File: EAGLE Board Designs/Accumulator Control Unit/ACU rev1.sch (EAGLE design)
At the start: 177 parts, among them J1 CONNECTOR-CAN_MF_T_V_, J2 CONNECTOR-8_MF_T_V_, J3 CONNECTOR-8_MF_T_V_, J4 CONNECTOR-2_MF_T_V_, J5 CONNECTOR-12_MF_T_V_, Q1 TRANSISTOR_N_MOS__PMV15ENEA, Q2 TRANSISTOR_N_MOS__PMV15ENEA, T1 TRANSFORMER_HM2112ZNLT_AIRGAP, U10 OPAMP_1_CHANNEL_OPA991, U11 LOGICGATE_AND_DCK3, U12 OPAMP_1_CHANNEL_OPA991, U13 OPAMP_1_CHANNEL_OPA991, U14 OPAMP_1_CHANNEL_OPA991, U15 LOGICGATE_AND_DCK3, U18 OPAMP_1_CHANNEL_OPA991, U19 MAX7404, U2 ADG1423, U20 OPAMP_1_CHANNEL_OPA991, U22 OPAMP_1_CHANNEL_OPA991, U25 TCAN1051HQV-Q1, U26 MAX7404, U27 OPAMP_1_CHANNEL_OPA991, U28 MAX7404, U29 OPAMP_1_CHANNEL_OPA991, U3 LM555, U30 MAX7404, U4 OPAMP_1_CHANNEL_OPA991, U5 LTC6820, U6 ADM823, U7 OPAMP_1_CHANNEL_OPA991, U8 LOGICGATE_AND_DCK3, U9 OPAMP_1_CHANNEL_OPA991

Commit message: pack+ and ts+ filtering
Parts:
- added D14: LED_0603_GREEN, HyTechDevices - Copy:LED_0603_GREEN
- added R71: RESISTOR_0603_470, HyTechDevices - Copy:RESISTOR_0603_470
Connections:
- new net N$14: D14.A, R71.1
- net +3V3: now also R71.2
- net GND: now also D14.C
- net IMD_OK_TEENSY: now also A1.A2; no longer A1.A4
- net PACK+_FILTERED: now also A1.A4; no longer A1.A3
- net TEENSY_OK: now also A1.D4; no longer A1.D8
- net TS+_OUT_FILTERED: now also A1.A3; no longer A1.A2
- net WATCHDOG_INPUT: now also A1.D5; no longer A1.D9
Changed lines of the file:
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@@
 <part name="P9" library="HyTechSupplies" deviceset="GND" device=""/>
 <part name="P3" library="HyTechSupplies" deviceset="+12V" device=""/>
+<part name="P45" library="HyTechSupplies" deviceset="GND" device=""/>
+<part name="P44" library="HyTechSupplies" deviceset="+3V3" device=""/>
+<part name="D14" library="HyTechDevices - Copy" deviceset="LED_?_*" device="0603" technology="GREEN"/>
+<part name="R71" library="HyTechDevices - Copy" deviceset="RESISTOR_?_*" device="0603" technology="470"/>
 </parts>
 <sheets>
@@
 <attribute name="VALUE" x="53.34" y="120.65" size="1.27" layer="96" align="bottom-center"/>
 </instance>
+<instance part="P45" gate="1" x="238.76" y="170.18" smashed="yes">
+<attribute name="VALUE" x="238.76" y="168.91" size="1.27" layer="96" align="top-center"/>
+</instance>
+<instance part="P44" gate="G$1" x="238.76" y="203.2" smashed="yes">
+<attribute name="VALUE" x="238.76" y="204.47" size="1.27" layer="96" align="bottom-center"/>
+</instance>
+<instance part="D14" gate="LED" x="238.76" y="177.8" smashed="yes" rot="R270">
+<attribute name="COLOR" x="236.982" y="179.07" size="1.27" layer="95" rot="R270" align="top-center"/>
+<attribute name="NAME" x="242.316" y="179.07" size="1.27" layer="96" rot="R270" align="bottom-center"/>
+</instance>
+<instance part="R71" gate="G$1" x="238.76" y="193.04" smashed="yes" rot="R90">
+<attribute name="NAME" x="237.49" y="191.77" size="1.27" layer="95" rot="R90" align="bottom-center"/>
+<attribute name="RESISTANCE" x="240.03" y="191.77" size="1.27" layer="96" rot="R90" align="top-center"/>
+</instance>
 </instances>
 <busses>
@@
 <pinref part="U$1" gate="G$1" pin="6"/>
 </segment>
+<segment>
+<wire x1="238.76" y1="175.26" x2="238.76" y2="172.72" width="0.1524" layer="91"/>
+<pinref part="P45" gate="1" pin="GND"/>
+<pinref part="D14" gate="LED" pin="C"/>
+</segment>
 </net>
 <net name="+12V" class="0">
@@
 <pinref part="A3" gate="G$1" pin="OUT"/>
 </segment>
+<segment>
+<wire x1="238.76" y1="200.66" x2="238.76" y2="195.58" width="0.1524" layer="91"/>
+<pinref part="P44" gate="G$1" pin="+3V3"/>
+<pinref part="R71" gate="G$1" pin="2"/>
+</segment>
 </net>
 <net name="PRECHARGE_OK" class="0">
@@
 </segment>
 </net>
+<net name="N$14" class="0">
+<segment>
+<wire x1="238.76" y1="187.96" x2="238.76" y2="182.88" width="0.1524" layer="91"/>
+<pinref part="D14" gate="LED" pin="A"/>
+<pinref part="R71" gate="G$1" pin="1"/>
+</segment>
+</net>
 </nets>
 </sheet>
@@
 </segment>
 <segment>
-<pinref part="A1" gate="G$1" pin="A4"/>
-<wire x1="48.26" y1="160.02" x2="45.72" y2="160.02" width="0.1524" layer="91"/>
-<label x="45.72" y="160.02" size="1.27" layer="95" rot="R180" xref="yes"/>
+<wire x1="48.26" y1="165.1" x2="45.72" y2="165.1" width="0.1524" layer="91"/>
+<label x="45.72" y="165.1" size="1.27" layer="95" rot="R180" xref="yes"/>
+<pinref part="A1" gate="G$1" pin="A2"/>
 </segment>
 </net>
@@
 </segment>
 <segment>
-<pinref part="A1" gate="G$1" pin="D9"/>
-<wire x1="73.66" y1="162.56" x2="88.9" y2="162.56" width="0.1524" layer="91"/>
-<label x="88.9" y="162.56" size="1.27" layer="95" xref="yes"/>
+<wire x1="73.66" y1="152.4" x2="88.9" y2="152.4" width="0.1524" layer="91"/>
+<label x="88.9" y="152.4" size="1.27" layer="95" xref="yes"/>
+<pinref part="A1" gate="G$1" pin="D5"/>
 </segment>
 </net>
@@
 </segment>
 </net>
-<net name="TS+_OUT_FILTERED" class="0">
-<segment>
-<pinref part="A1" gate="G$1" pin="A2"/>
-<wire x1="48.26" y1="165.1" x2="43.18" y2="165.1" width="0.1524" layer="91"/>
-<label x="43.18" y="165.1" size="1.27" layer="95" rot="R180" xref="yes"/>
-</segment>
-</net>
-<net name="PACK+_FILTERED" class="0">
-<segment>
-<pinref part="A1" gate="G$1" pin="A3"/>
-<wire x1="48.26" y1="162.56" x2="45.72" y2="162.56" width="0.1524" layer="91"/>
-<label x="45.72" y="162.56" size="1.27" layer="95" rot="R180" xref="yes"/>
-</segment>
-</net>
 <net name="N$40" class="0">
 <segment>
@@
 <net name="TEENSY_OK" class="0">
 <segment>
-<pinref part="A1" gate="G$1" pin="D8"/>
-<wire x1="73.66" y1="160.02" x2="88.9" y2="160.02" width="0.1524" layer="91"/>
-<label x="88.9" y="160.02" size="1.27" layer="95" xref="yes"/>
-</segment>
-<segment>
 <pinref part="U6" gate="G$1" pin="!MR!"/>
 <wire x1="215.9" y1="91.44" x2="208.28" y2="91.44" width="0.1524" layer="91"/>
@@
 <label x="190.5" y="91.44" size="1.27" layer="95" rot="R180" xref="yes"/>
 </segment>
+<segment>
+<wire x1="73.66" y1="149.86" x2="88.9" y2="149.86" width="0.1524" layer="91"/>
+<label x="88.9" y="149.86" size="1.27" layer="95" xref="yes"/>
+<pinref part="A1" gate="G$1" pin="D4"/>
+</segment>
 </net>
 <net name="N$13" class="0">
@@
 </segment>
 </net>
+<net name="TS+_OUT_FILTERED" class="0">
+<segment>
+<wire x1="48.26" y1="162.56" x2="45.72" y2="162.56" width="0.1524" layer="91"/>
+<label x="45.72" y="162.56" size="1.27" layer="95" rot="R180" xref="yes"/>
+<pinref part="A1" gate="G$1" pin="A3"/>
+</segment>
+</net>
+<net name="PACK+_FILTERED" class="0">
+<segment>
+<wire x1="48.26" y1="160.02" x2="45.72" y2="160.02" width="0.1524" layer="91"/>
+<label x="45.72" y="160.02" size="1.27" layer="95" rot="R180" xref="yes"/>
+<pinref part="A1" gate="G$1" pin="A4"/>
+</segment>
+</net>

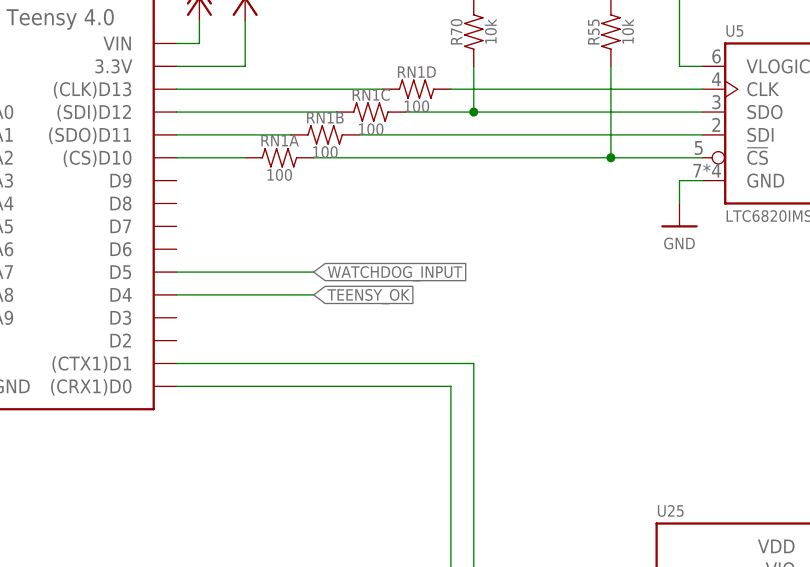
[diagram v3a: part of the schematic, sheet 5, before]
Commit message: routed shutdown optocouplers
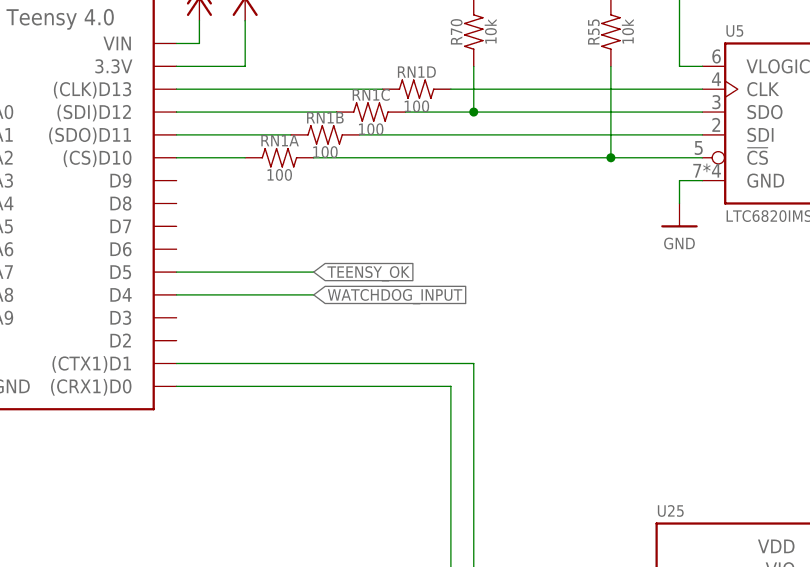
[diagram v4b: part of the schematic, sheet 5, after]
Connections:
- net TEENSY_OK: now also A1.D5; no longer A1.D4
- net WATCHDOG_INPUT: now also A1.D4; no longer A1.D5
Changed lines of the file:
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@@
 <drawing>
 <settings>
-<setting alwaysvectorfont="yes"/>
+<setting alwaysvectorfont="no"/>
 <setting verticaltext="up"/>
 </settings>
@@
 </segment>
 <segment>
-<wire x1="73.66" y1="152.4" x2="88.9" y2="152.4" width="0.1524" layer="91"/>
-<label x="88.9" y="152.4" size="1.27" layer="95" xref="yes"/>
-<pinref part="A1" gate="G$1" pin="D5"/>
+<wire x1="73.66" y1="149.86" x2="88.9" y2="149.86" width="0.1524" layer="91"/>
+<label x="88.9" y="149.86" size="1.27" layer="95" xref="yes"/>
+<pinref part="A1" gate="G$1" pin="D4"/>
 </segment>
 </net>
@@
 </segment>
 <segment>
-<wire x1="73.66" y1="149.86" x2="88.9" y2="149.86" width="0.1524" layer="91"/>
-<label x="88.9" y="149.86" size="1.27" layer="95" xref="yes"/>
-<pinref part="A1" gate="G$1" pin="D4"/>
+<wire x1="73.66" y1="152.4" x2="88.9" y2="152.4" width="0.1524" layer="91"/>
+<label x="88.9" y="152.4" size="1.27" layer="95" xref="yes"/>
+<pinref part="A1" gate="G$1" pin="D5"/>
 </segment>
 </net>

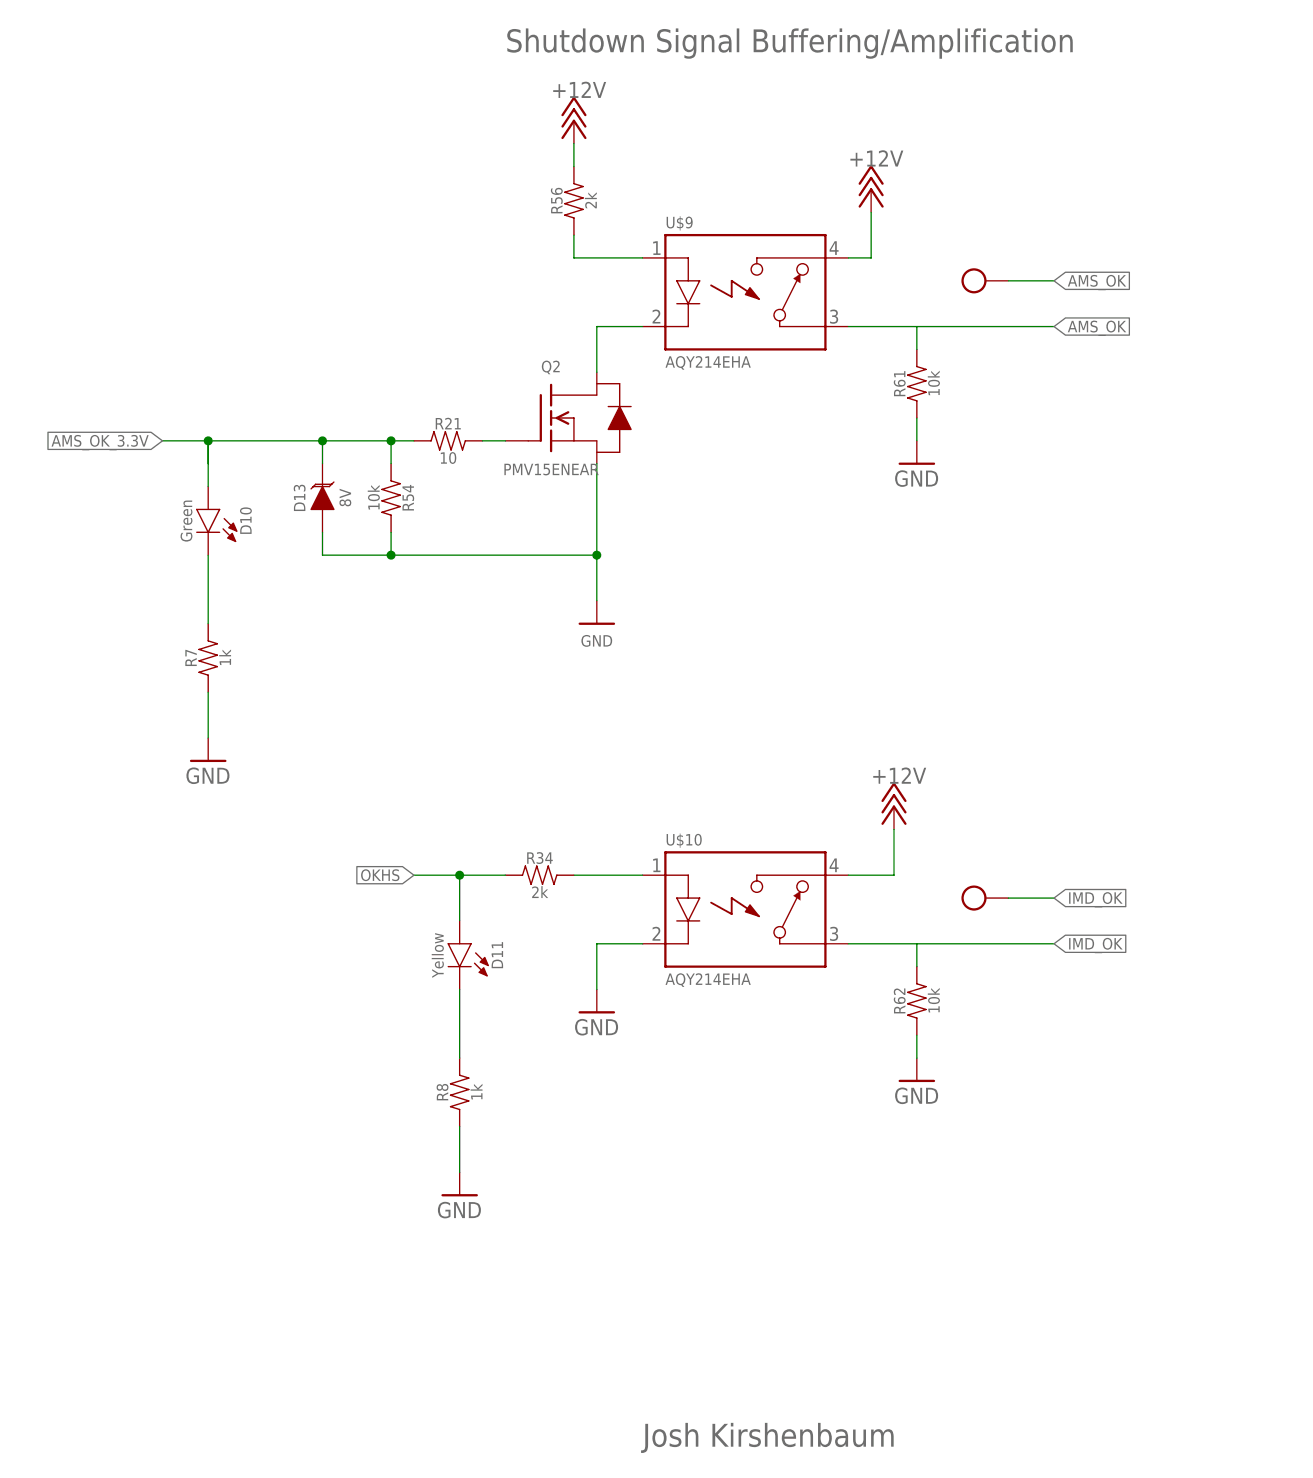
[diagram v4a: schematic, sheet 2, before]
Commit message: passes drc
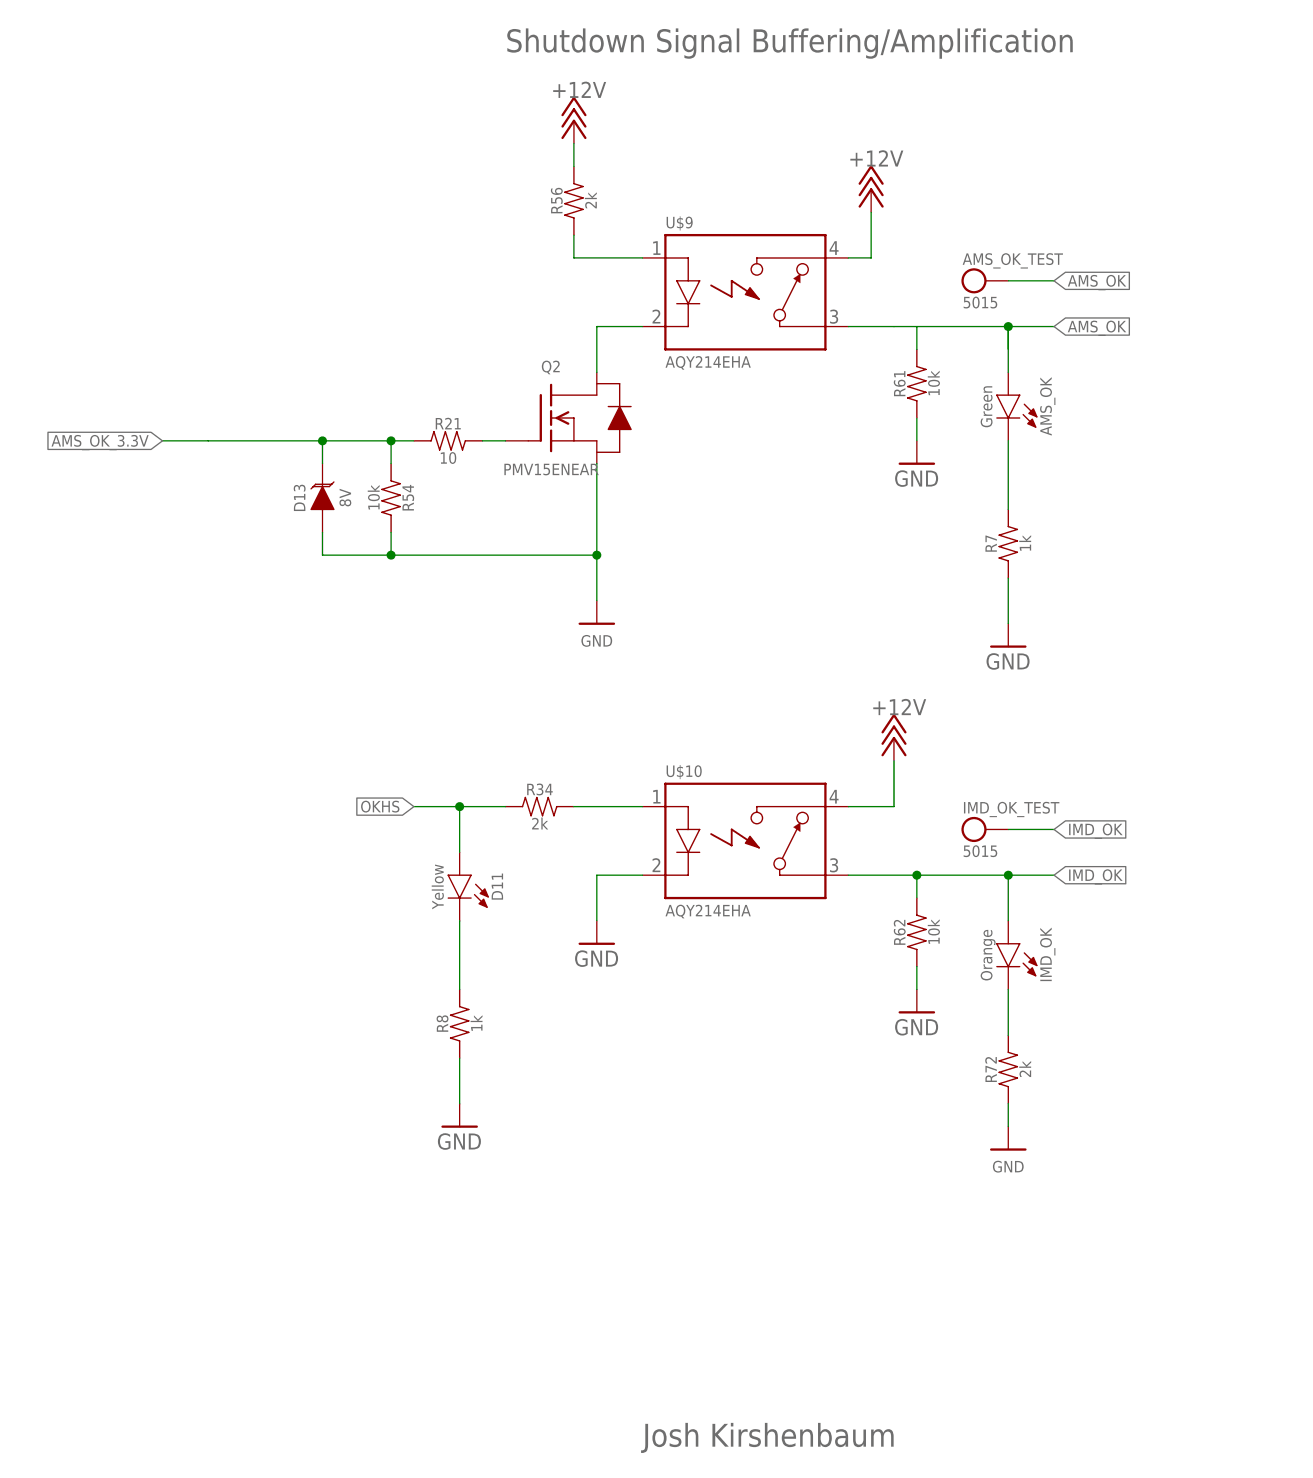
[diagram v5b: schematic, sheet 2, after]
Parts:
- removed $$U$12, U$13: TEST_POINTMICRO_MINIATURE, HyTechDevices:TEST_POINTMICRO_MINIATURE
- removed D10: LED_0603_GREEN, HyTechDevices - Copy:LED_0603_GREEN
- removed TP25: TEST_POINT, HyTechDevices:TEST_POINT
- added AMS_OK: LED_0603_GREEN, HyTechDevices - Copy:LED_0603_GREEN
- added AMS_OK_TEST, CURRENT_REF, CURRENT_SENSE, IMD_OK_TEST, PACK+_OUT_TEST, TS+_OUT_TEST, WATCHDOG_OK: TEST_POINT, HyTechDevices - Copy:TEST_POINT
- added C14, C15: CAPACITOR_0603_10V_0.1UF, HyTechDevices - Copy:CAPACITOR_0603_10V_0.1UF
- added IMD_OK: LED_0603_ORANGE, HyTechDevices - Copy:LED_0603_ORANGE
- added R72: RESISTOR_0603_2K, HyTechDevices:RESISTOR_0603_2K
- renumbered D14 to 3.3V, D2 to 5V, D3 to 12V, TP1 to 12V_TEST, TP2 to 5V_TEST, TP3 to 3.3V_TEST, TP4 to GND_TEST, TP5 to BSPD_CURRENT
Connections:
- removed net AMS_OK1: R62.2
- new net N$27: IMD_OK.C, R72.2
- net +3V3: now also C15.2
- net +5V: now also C14.1
- net AMS_OK: now also AMS_OK.A, AMS_OK_TEST.P$1; no longer U$13.P$1
- net AMS_OK_3.3V: no longer D10.A
- net CURRENT: now also CURRENT_SENSE.P$1
- net CURRENT_REF: now also CURRENT_REF.P$1
- net GND: now also C14.2, C15.1, R72.1
- net IMD_OK: now also IMD_OK.A, IMD_OK_TEST.P$1, R62.2; no longer $$U$12.P$1
- net N$17: now also AMS_OK.C; no longer D10.C
- net PACK+_OUT: now also PACK+_OUT_TEST.P$1; no longer TP25.P$1
- net TS+_OUT: now also TS+_OUT_TEST.P$1
- net WATCHDOG_INPUT: now also WATCHDOG_OK.P$1
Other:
- moved on the sheet: D11, R34, R62, R7, R8, U$10
